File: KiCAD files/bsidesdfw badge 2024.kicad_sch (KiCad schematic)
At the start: 27 parts, among them Q1 BC548, SW1 SW_SPDT_312, U1 NE555P, U2 74HC595

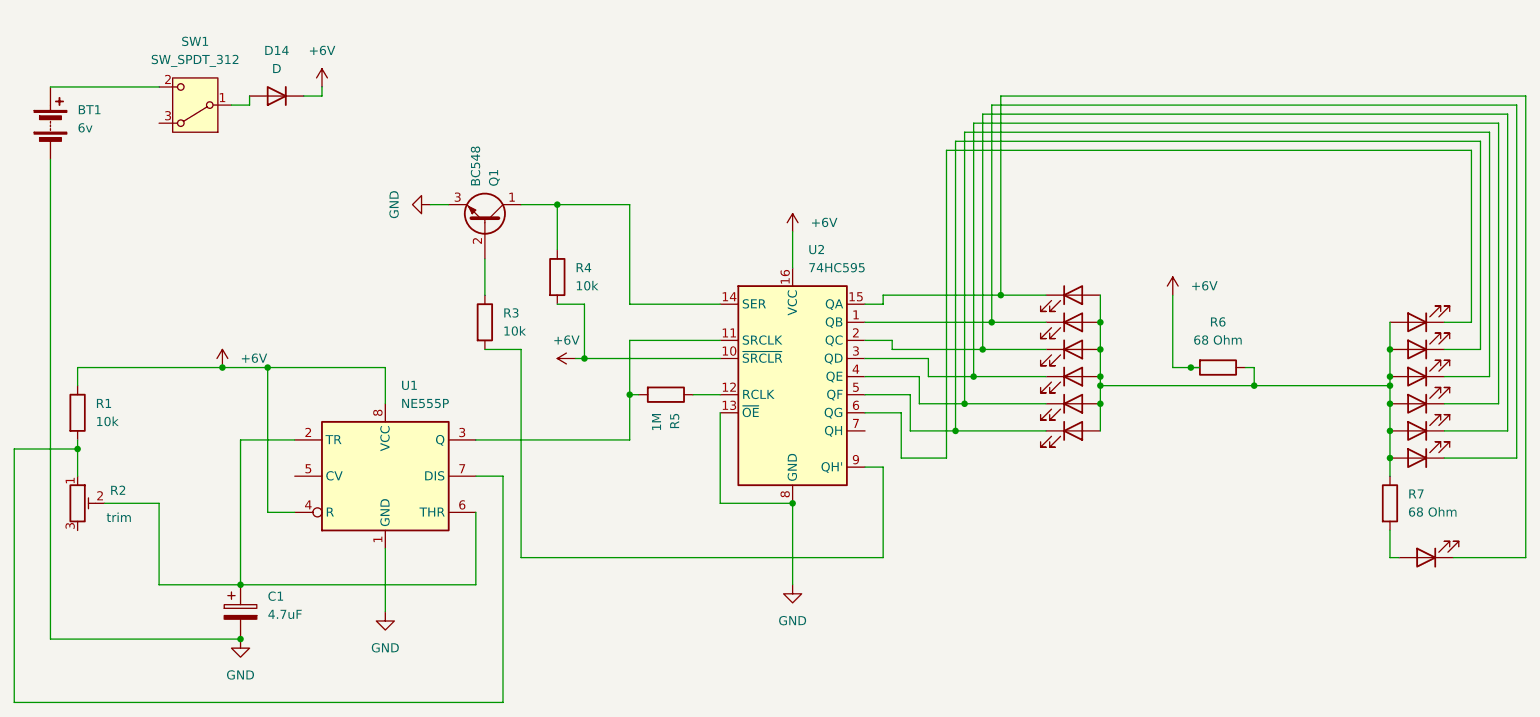
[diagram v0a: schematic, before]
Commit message: trace rerouting; some silkscreen cleanup. Need to remake the aesthetic mask to fix the dots overlapping the LEDs
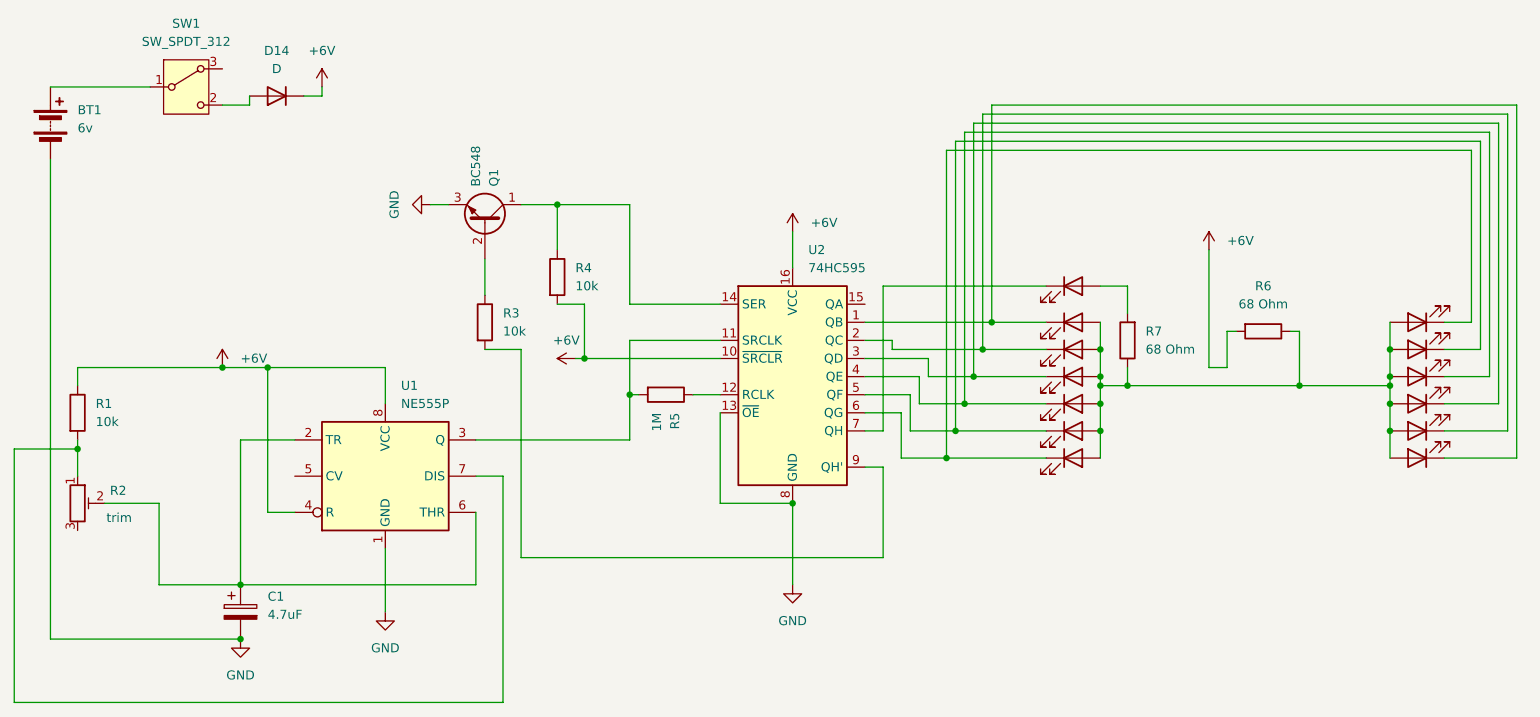
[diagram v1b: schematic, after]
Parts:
- removed D1: ~, LED_THT:LED_D5.0mm, symbol Device:LED
- added D6: ~, LED_THT:LED_D5.0mm, symbol Device:LED
- renumbered D2 to D1, D3 to D2, D4 to D3, D5 to D4, D6 to D5
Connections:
- net at D1.2 (A), D10.2 (A), D11.2 (A)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: now also D6.2 (A)
- net at BT1.1 (+): now also SW1.1 (B); no longer SW1.2 (C)
- net at U2.15 (QA): no longer D13.1 (K)
- net at D12.1 (K), U2.6 (QG): now also D6.1 (K)
- net at U2.7 (QH): now also D13.1 (K)
- net at D14.2 (A): now also SW1.2 (C); no longer SW1.1 (B)
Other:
- moved on the sheet: R6, SW1

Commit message: fixed a trace exposure from resizing battery pads; cleaned up and exported schematic to SVG for documentation.
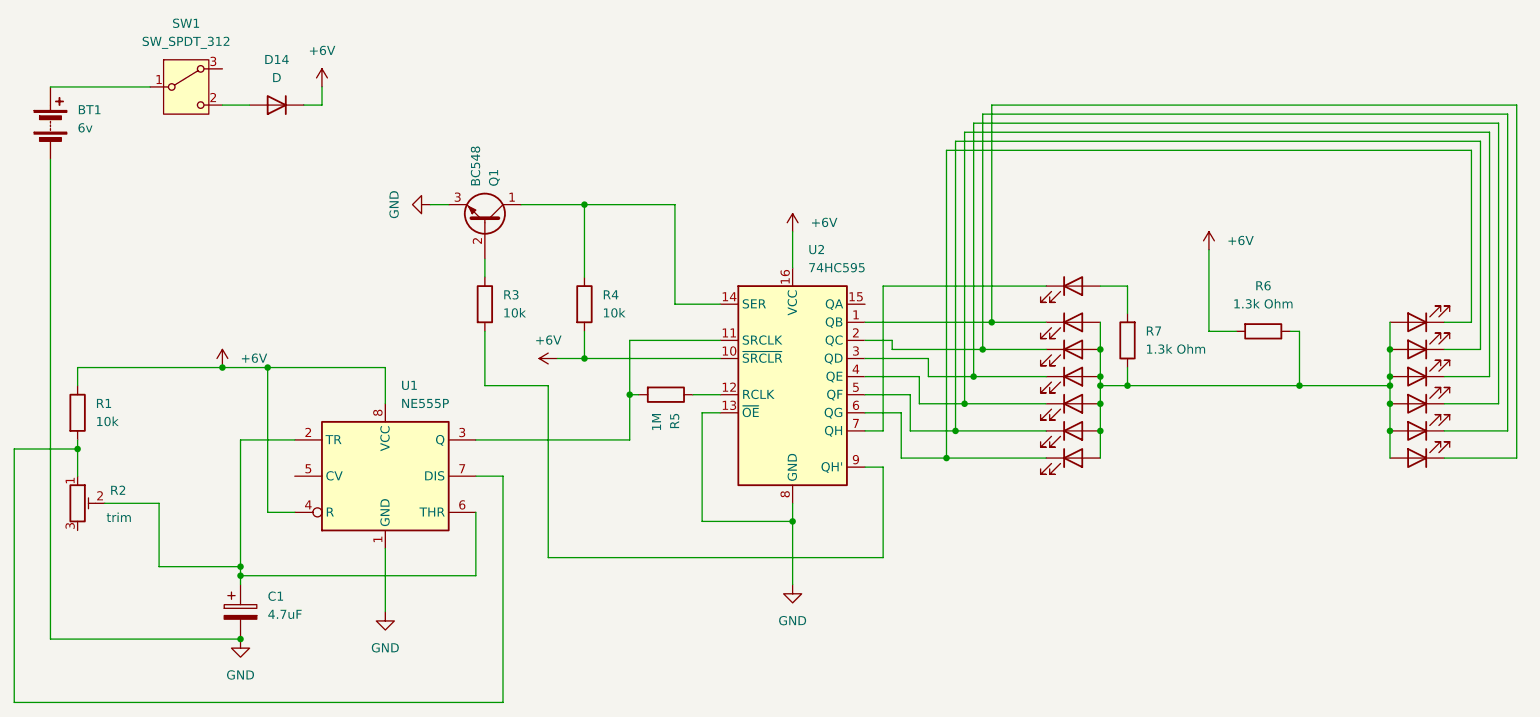
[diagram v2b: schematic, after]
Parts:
- R6, R7: value 68 Ohm -> 1.3k Ohm
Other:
- moved on the sheet: D14, R3, R4
